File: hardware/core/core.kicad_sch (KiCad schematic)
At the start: 39 parts, among them J1 9V_IN, J2 LCD, J3 MIDI IN, J4 MIDI OUT 1, J5 MIDI OUT 2, J6 MIDI OUT 3, J7 MIDI OUT 4, SW1 FS, SW2 FS, SW3 FS, SW4 FS, SW5 FS, SW6 FS, SW7 FS, SW8 FS, U1 ESP32-S3-DevKitC, U2 L7805, U3 6N137S

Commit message: Prompt is too long
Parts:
- removed U3: 6N137S, 4ms_Package_SSOP:SOP-8_6.605x9.655mm_P2.54mm, symbol 4ms_IC:6N137
- added D10: 1N5817, Diode_THT:D_DO-41_SOD81_P10.16mm_Horizontal, symbol Diode:1N5817
- added RV1: 10K, Potentiometer_THT:Potentiometer_Bourns_3296Y_Vertical, symbol Device:R_Potentiometer
- added U3: 6N137, Package_DIP:DIP-8_W7.62mm, symbol Isolator:6N137
- C1: footprint (none) -> Capacitor_THT:C_Rect_L7.0mm_W4.5mm_P5.00mm
- C2: footprint (none) -> Capacitor_THT:C_Rect_L7.0mm_W2.5mm_P5.00mm
- J1: footprint (none) -> Connector_BarrelJack:BarrelJack_Horizontal
- J2: footprint (none) -> midilord:4004A
- J3, J4: footprint (none) -> midilord:DIN5_180
- J5, J6, J7: footprint (none) -> Connector_Audio:Jack_6.35mm_Neutrik_NMJ6HFD2-AU_Horizontal
- R1: value R -> 220R; footprint (none) -> Resistor_THT:R_Axial_DIN0204_L3.6mm_D1.6mm_P7.62mm_Horizontal
- R10: renamed from R2; value R -> 1K; footprint (none) -> Resistor_THT:R_Axial_DIN0204_L3.6mm_D1.6mm_P7.62mm_Horizontal
- R2: renamed from R5; footprint (none) -> Resistor_THT:R_Axial_DIN0204_L3.6mm_D1.6mm_P7.62mm_Horizontal
- R3: renamed from R6; footprint (none) -> Resistor_THT:R_Axial_DIN0204_L3.6mm_D1.6mm_P7.62mm_Horizontal
- R4: renamed from R7; footprint (none) -> Resistor_THT:R_Axial_DIN0204_L3.6mm_D1.6mm_P7.62mm_Horizontal
- R5: renamed from R3; footprint (none) -> Resistor_THT:R_Axial_DIN0204_L3.6mm_D1.6mm_P7.62mm_Horizontal
- R6: renamed from R8; footprint (none) -> Resistor_THT:R_Axial_DIN0204_L3.6mm_D1.6mm_P7.62mm_Horizontal
- R7: renamed from R9; footprint (none) -> Resistor_THT:R_Axial_DIN0204_L3.6mm_D1.6mm_P7.62mm_Horizontal
- R8: renamed from R10; footprint (none) -> Resistor_THT:R_Axial_DIN0204_L3.6mm_D1.6mm_P7.62mm_Horizontal
- R9: renamed from R4; footprint (none) -> Resistor_THT:R_Axial_DIN0204_L3.6mm_D1.6mm_P7.62mm_Horizontal
- SW1, SW2, SW3, SW4, SW5, SW6, SW7, SW8: footprint (none) -> Connector_PinHeader_2.54mm:PinHeader_1x02_P2.54mm_Vertical
- U1: footprint PCM_Espressif:ESP32-S3-DevKitC -> Espressif:ESP32-S3-DevKitC
- U2: footprint (none) -> Package_TO_SOT_THT:TO-220-3_Vertical
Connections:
- net +5V: now also J2.14 (Pin_14), J2.17 (Pin_17), R10.1, RV1.1, U3.8 (VCC)
- net +9V: now also D10.2 (A); no longer C1.1, U2.1 (IN)
- net GND: now also J2.10 (Pin_10), J2.13 (Pin_13), J2.18 (Pin_18), J2.5 (Pin_5), J2.6 (Pin_6), J2.7 (Pin_7), J2.8 (Pin_8), RV1.3, U3.5 (GND)
- net MCU_MIDI_IN: now reaches R10.2
- net MCU_MIDI_IN: now also U3.6 (VO)
- net at D9.1 (K): now also R1.2, U3.2 (A)
- net at D9.2 (A): now also J3.5, U3.3 (C)
- net E2: now reaches U1.12 (GPIO8/ADC1_CH7)
- net E2: now also J2.15 (Pin_15)
- net DB4: now reaches U1.15 (GPIO9/ADC1_CH8)
- net DB4: now also J2.4 (Pin_4)
- net DB5: now reaches U1.16 (GPIO10/ADC1_CH9)
- net DB5: now also J2.3 (Pin_3)
- net DB6: now reaches U1.17 (GPIO11/ADC2_CH0)
- net DB6: now also J2.2 (Pin_2)
- net DB7: now reaches U1.18 (GPIO12/ADC2_CH1)
- net DB7: now also J2.1 (Pin_1)
- net RS: now reaches U1.6 (GPIO6/ADC1_CH5)
- net RS: now also J2.11 (Pin_11)
- net E1: now reaches U1.7 (GPIO7/ADC1_CH6)
- net E1: now also J2.9 (Pin_9)
- net at J3.4: now also R1.1
- net at J2.12 (Pin_12): now also RV1.2
- new net: C1.1, D10.1 (K), U2.1 (IN)
- no-connect marks 0 -> 1
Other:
- moved on the sheet: J1, J3, R1, R10

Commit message: Prompt is too long
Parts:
- removed C1: 220n, Capacitor_THT:C_Rect_L7.0mm_W4.5mm_P5.00mm, symbol Device:C
- removed D10: 1N5817, Diode_THT:D_DO-41_SOD81_P10.16mm_Horizontal, symbol Diode:1N5817
- removed U1: ESP32-S3-DevKitC, Espressif:ESP32-S3-DevKitC, symbol Espressif:ESP32-S3-DevKitC
- removed U2: L7805, Package_TO_SOT_THT:TO-220-3_Vertical, symbol Regulator_Linear:L7805
- added C1: 330u, Capacitor_THT:CP_Radial_D10.0mm_P5.00mm, symbol Device:C_Polarized
- added C3: 100n, Capacitor_THT:C_Rect_L7.0mm_W2.5mm_P5.00mm, symbol Device:C
- added C4: 100u, Capacitor_THT:CP_Radial_D8.0mm_P3.50mm, symbol Device:C_Polarized
- added C5: 220u, Capacitor_THT:CP_Radial_D8.0mm_P3.50mm, symbol Device:C_Polarized
- added D10, D3, D4, D5, D6, D7, D8, D9: WS2812B, LED_THT:LED_D5.0mm-4_RGB_Wide_Pins, symbol LED:WS2812B
- added D2: 1N5822, Diode_THT:D_DO-201AD_P15.24mm_Horizontal, symbol Diode:1N5822
- added IC1: LD1117-3.3V-SOT223, 4ms_Package_SOT:SOT223, symbol 4ms_Regulator:LD1117-3.3V-SOT223
- added J8: USB_C_Receptacle_USB2.0_16P, Connector_USB:USB_C_Receptacle_GCT_USB4085, symbol Connector:USB_C_Receptacle_USB2.0_16P
- added L1: 33uH, Inductor_THT:L_Radial_D9.5mm_P5.00mm_Fastron_07HVP, symbol Device:L
- added R11, R12: 5.1K, Resistor_THT:R_Axial_DIN0204_L3.6mm_D1.6mm_P7.62mm_Horizontal, symbol Device:R
- added R13, R14: 22R, Resistor_THT:R_Axial_DIN0204_L3.6mm_D1.6mm_P7.62mm_Horizontal, symbol Device:R
- added U1: LM2596S-5, Package_TO_SOT_SMD:TO-263-5_TabPin3, symbol Regulator_Switching:LM2596S-5
- added U3: ESP32-S3-WROOM-1, RF_Module:ESP32-S3-WROOM-1, symbol RF_Module:ESP32-S3-WROOM-1
- added U5: USBLC6-2SC6, Package_TO_SOT_SMD:SOT-23-6, symbol Power_Protection:USBLC6-2SC6
- SW1, SW8: footprint Connector_PinHeader_2.54mm:PinHeader_1x02_P2.54mm_Vertical -> midilord:Footswitch
- SW2: renamed from SW3; footprint Connector_PinHeader_2.54mm:PinHeader_1x02_P2.54mm_Vertical -> midilord:Footswitch
- SW3: renamed from SW5; footprint Connector_PinHeader_2.54mm:PinHeader_1x02_P2.54mm_Vertical -> midilord:Footswitch
- SW4: renamed from SW7; footprint Connector_PinHeader_2.54mm:PinHeader_1x02_P2.54mm_Vertical -> midilord:Footswitch
- SW5: renamed from SW2; footprint Connector_PinHeader_2.54mm:PinHeader_1x02_P2.54mm_Vertical -> midilord:Footswitch
- SW6: renamed from SW4; footprint Connector_PinHeader_2.54mm:PinHeader_1x02_P2.54mm_Vertical -> midilord:Footswitch
- SW7: renamed from SW6; footprint Connector_PinHeader_2.54mm:PinHeader_1x02_P2.54mm_Vertical -> midilord:Footswitch
- renumbered D9 to D1, D1 to D11, D3 to D12, D5 to D13, D7 to D14, D2 to D15, D4 to D16, D6 to D17, D8 to D18, J3 to J2, J4 to J3, J5 to J4, J6 to J5, J7 to J6, J2 to J7, R4 to R10, R10 to R2, R9 to R3, R5 to R4, R6 to R5, R2 to R6, R3 to R8, R8 to R9, U3 to U2
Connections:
- net +3.3V: now also C4.1, IC1.2 (OUT), U3.2 (3V3)
- net +5V: now also C3.1, C5.1, D10.1 (VDD), D3.1 (VDD), D4.1 (VDD), D5.1 (VDD), D6.1 (VDD), D7.1 (VDD), D8.1 (VDD), D9.1 (VDD), IC1.3 (IN), L1.2, U1.4 (FB), U5.5 (VBUS); no longer C2.1
- net +9V: now also C2.1, C1.1, U1.1 (VIN)
- net DB4: now also U3.15 (IO3)
- net DB5: now also U3.18 (IO10)
- net DB6: now also U3.16 (IO46)
- net DB7: now also U3.17 (IO9)
- net E1: now also U3.19 (IO11)
- net E2: now also U3.21 (IO13)
- net GND: now also C1.2, C3.2, C4.2, C5.2, D10.3 (VSS), D2.2 (A), D3.3 (VSS), D4.3 (VSS), D5.3 (VSS), D6.3 (VSS), D7.3 (VSS), D8.3 (VSS), D9.3 (VSS), IC1.1 (GND), J8.A1 (GND), J8.A12 (GND), J8.B1 (GND), J8.B12 (GND), J8.S1 (SHIELD), R11.2, R12.2, U1.3 (GND), U1.5 (~{ON}/OFF), U3.1 (GND), U3.40 (GND), U3.41 (GND), U5.2 (GND)
- net RS: now also U3.20 (IO12)
- net at D12.2 (A): now also SW2.1; no longer SW2.2
- net at D11.2 (A): now also SW1.1; no longer SW1.2
- net at D18.2 (A): now also SW8.1; no longer SW8.2
- net at D17.2 (A): now also SW7.1; no longer SW7.2
- net MCU_MIDI_IN renamed MIDI_IN
- net MCU_MIDI_OUT1 renamed MIDI_OUT1
- net MCU_MIDI_OUT2 renamed MIDI_OUT2
- net MCU_MIDI_OUT3 renamed MIDI_OUT3
- net MCU_MIDI_OUT4 renamed MIDI_OUT4
- net c1 renamed C1
- net C1: now also SW1.2; no longer SW1.1
- net c2 renamed C2
- net C2: now also SW2.2; no longer SW2.1
- net c3 renamed C3
- net C3: now also SW7.2; no longer SW7.1
- net c4 renamed C4
- net C4: now also SW8.2; no longer SW8.1
- net r1 renamed R1
- net r2 renamed R2
- new net: D10.4 (DIN), D9.2 (DOUT)
- new net: J8.A4 (VBUS), J8.A9 (VBUS), J8.B4 (VBUS), J8.B9 (VBUS)
- new net: J8.A5 (CC1), R12.1
- new net: J8.B5 (CC2), R11.1
- new net: R13.1, U5.4 (I/O2)
- new net: R14.1, U5.6 (I/O1)
- new net: D2.1 (K), L1.1, U1.2 (OUT)
- new net: D6.2 (DOUT), D7.4 (DIN)
- new net: D5.2 (DOUT), D6.4 (DIN)
- new net: D8.2 (DOUT), D9.4 (DIN)
- new net: D3.2 (DOUT), D4.4 (DIN)
- new net: D4.2 (DOUT), D5.4 (DIN)
- new net: D7.2 (DOUT), D8.4 (DIN)
- new net D+: J8.A6 (D+), J8.B6 (D+), U5.3 (I/O2)
- new net D-: J8.A7 (D-), J8.B7 (D-), U5.1 (I/O1)
- new net DN: R14.2, U3.13 (USB_D-)
- new net DP: R13.2, U3.14 (USB_D+)
- new net MCU_LED: D3.4 (DIN)
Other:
- moved on the sheet: C2, D11, D12, D13, D14, D15, D16, D17, D18, J1, J7, RV1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

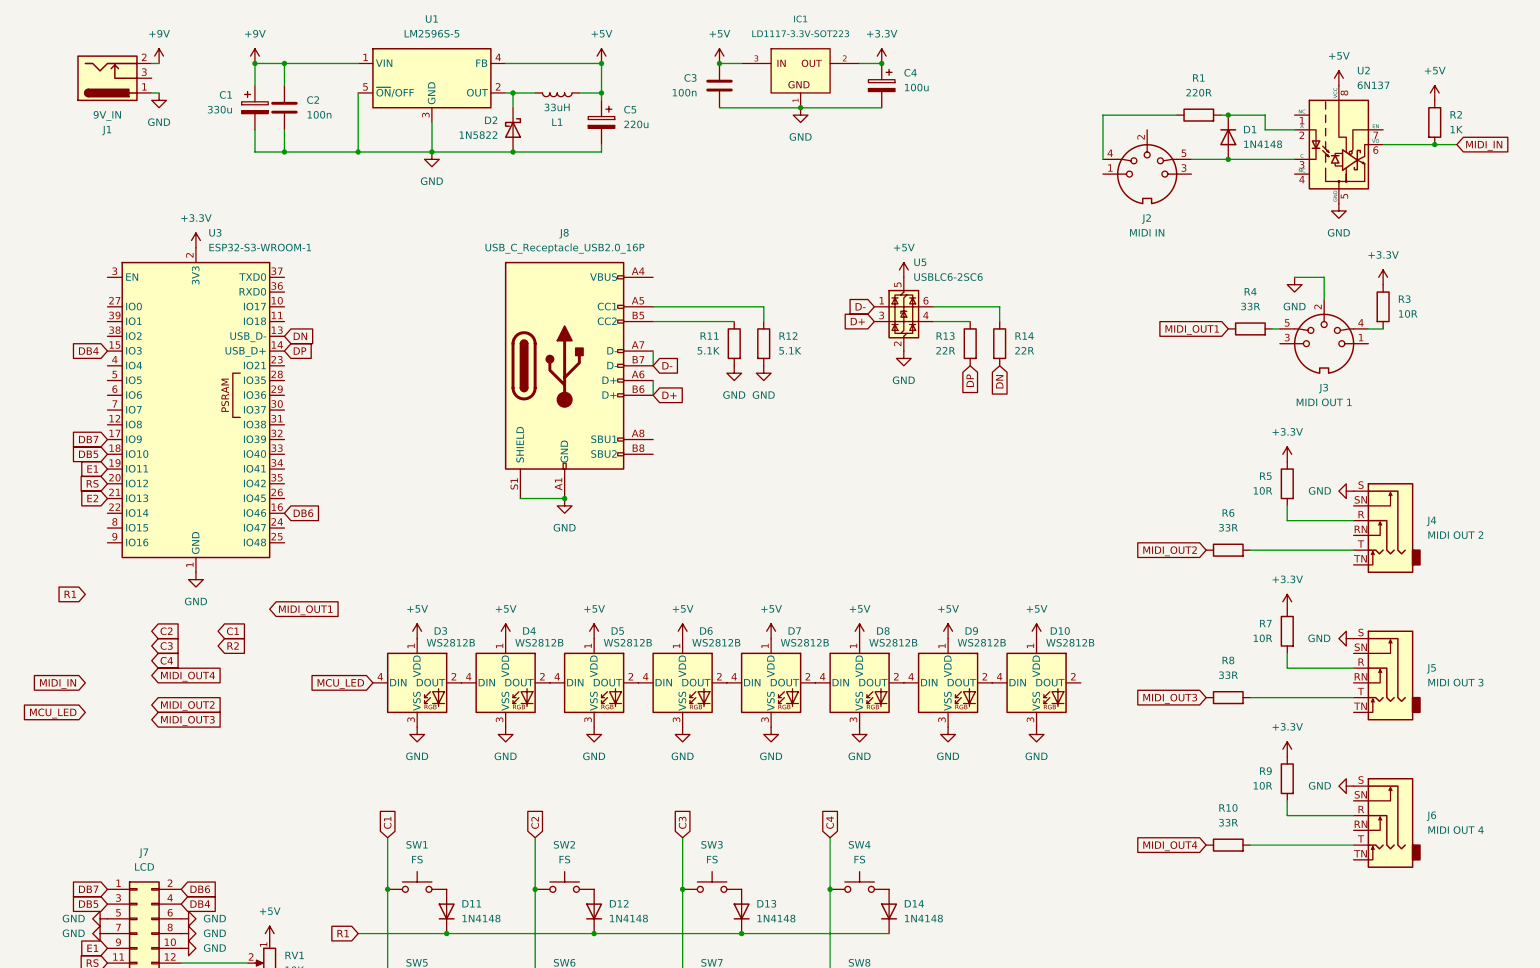
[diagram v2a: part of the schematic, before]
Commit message: Reduce PCB to 2-layer stackup and update design rules
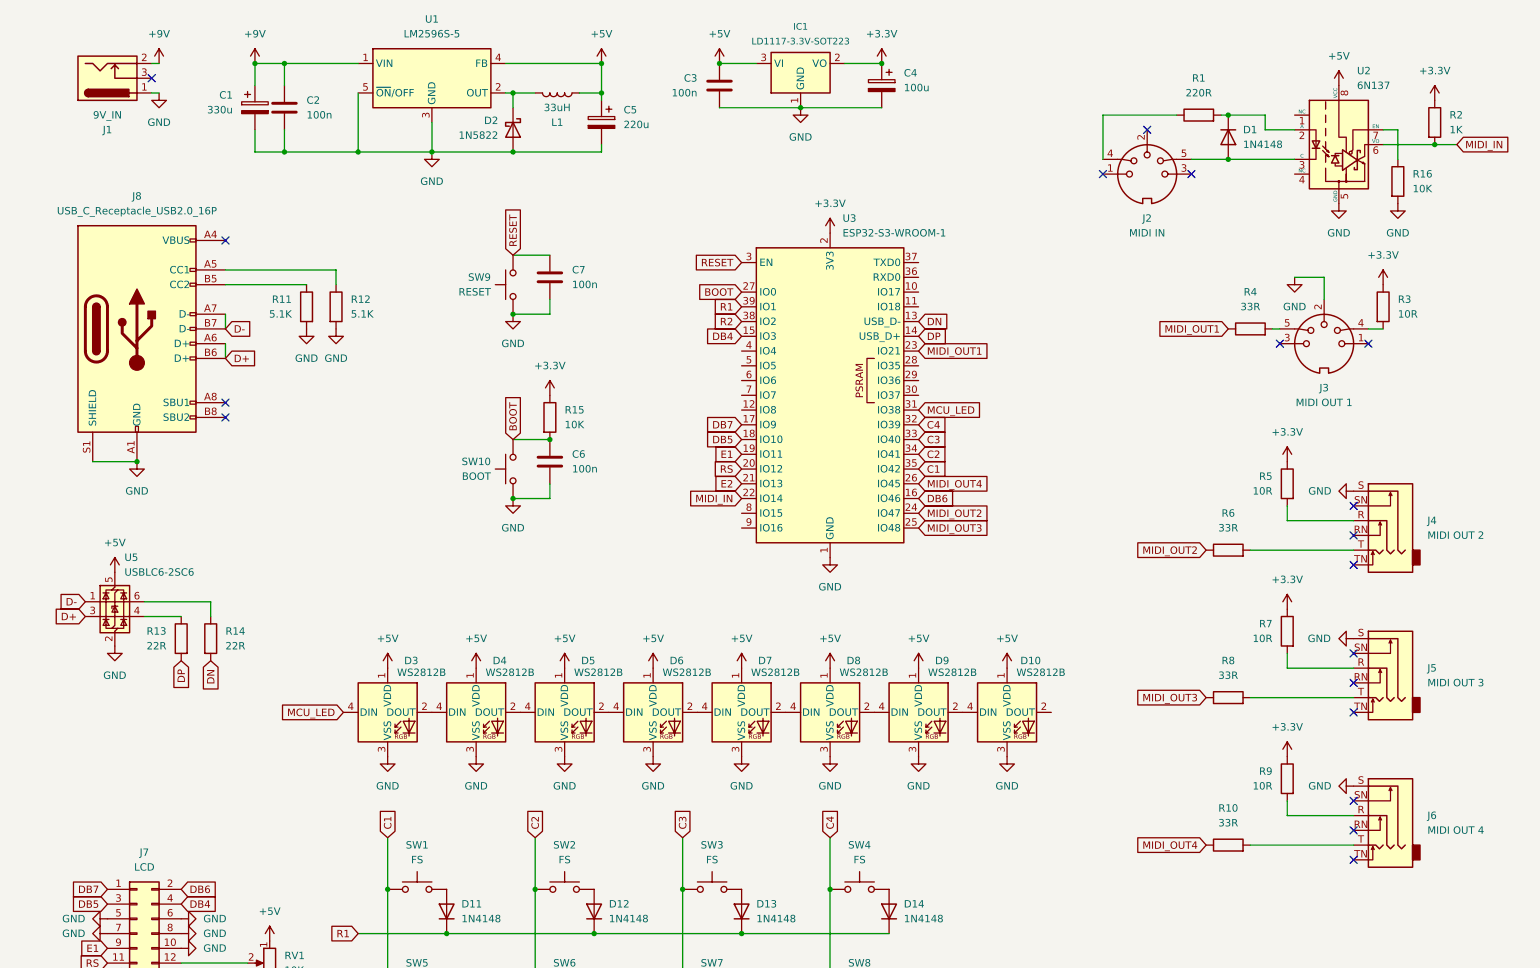
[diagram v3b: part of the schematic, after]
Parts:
- added C6, C7: 100n, Capacitor_THT:C_Rect_L7.0mm_W2.5mm_P5.00mm, symbol Device:C
- added R15, R16: 10K, Resistor_THT:R_Axial_DIN0204_L3.6mm_D1.6mm_P7.62mm_Horizontal, symbol Device:R
- added SW10: BOOT, Button_Switch_THT:SW_PUSH_1P1T_6x3.5mm_H5.0_APEM_MJTP1250, symbol Switch:SW_Push
- added SW9: RESET, Button_Switch_THT:SW_PUSH_1P1T_6x3.5mm_H5.0_APEM_MJTP1250, symbol Switch:SW_Push
- D10, D3, D4, D5, D6, D7, D8, D9: footprint LED_THT:LED_D5.0mm-4_RGB_Wide_Pins -> midilord:APA106
- IC1: footprint 4ms_Package_SOT:SOT223 -> Package_TO_SOT_SMD:SOT-223; symbol 4ms_Regulator:LD1117-3.3V-SOT223 -> Regulator_Linear:LD1117S33TR_SOT223
- J4, J5, J6: footprint Connector_Audio:Jack_6.35mm_Neutrik_NMJ6HFD2-AU_Horizontal -> midilord:CK635-006
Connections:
- net +3.3V: now also R2.1, R15.1
- net +5V: no longer R2.1
- net C1: now also U3.35 (IO42)
- net C2: now also U3.34 (IO41)
- net C3: now also U3.33 (IO40)
- net C4: now also U3.32 (IO39)
- net GND: now also C6.2, C7.2, R16.2, SW10.1, SW9.1
- net MCU_LED: now also U3.31 (IO38)
- net MIDI_IN: now also U3.22 (IO14)
- net MIDI_OUT1: now also U3.23 (IO21)
- net MIDI_OUT2: now also U3.24 (IO47)
- net MIDI_OUT3: now also U3.25 (IO48)
- net MIDI_OUT4: now also U3.26 (IO45)
- net R1: now also U3.39 (IO1)
- net R2: now also U3.38 (IO2)
- net BOOT: now reaches U3.27 (IO0)
- net BOOT: now also C6.1, R15.2, SW10.2
- net RESET: now reaches U3.3 (EN)
- net RESET: now also C7.1, SW9.2
- net at U2.7 (EN): now also R16.1
- no-connect marks 1 -> 19
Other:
- moved on the sheet: D10, D3, D4, D5, D6, D7, D8, D9, J8, R11, R12, R13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
